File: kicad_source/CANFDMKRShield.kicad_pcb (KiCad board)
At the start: 2 copper layers, 61.5 x 25 mm, 33 parts, among them CN1 ARDUINO_MKR, CN2 CONN_01X04, CN3 GH_SM04B-GHS-TB, CN4 GH_SM04B-GHS-TB, SW1 JS202011JCQN, U1 MCP2517FD, U2 SN65HVD232, U3 TPS54232, Y1 20MHz

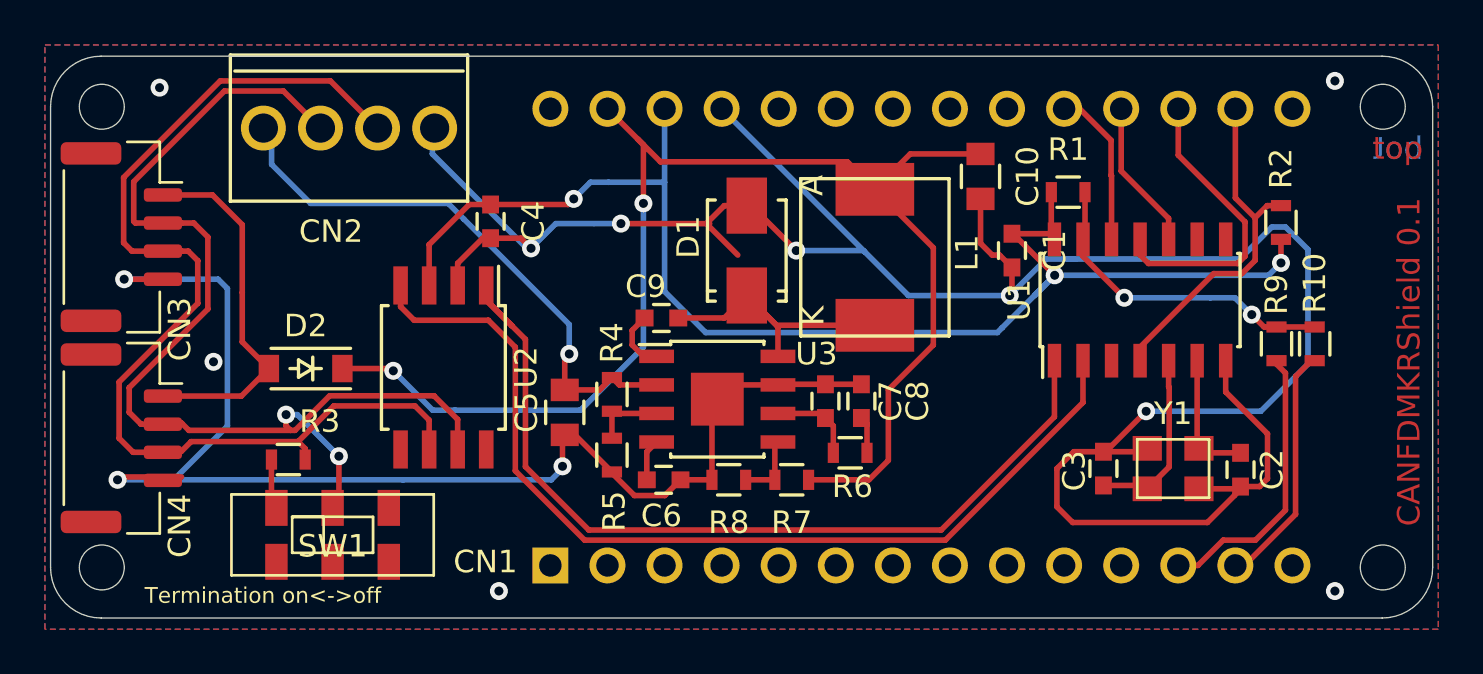
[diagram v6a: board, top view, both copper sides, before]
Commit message: updated layout
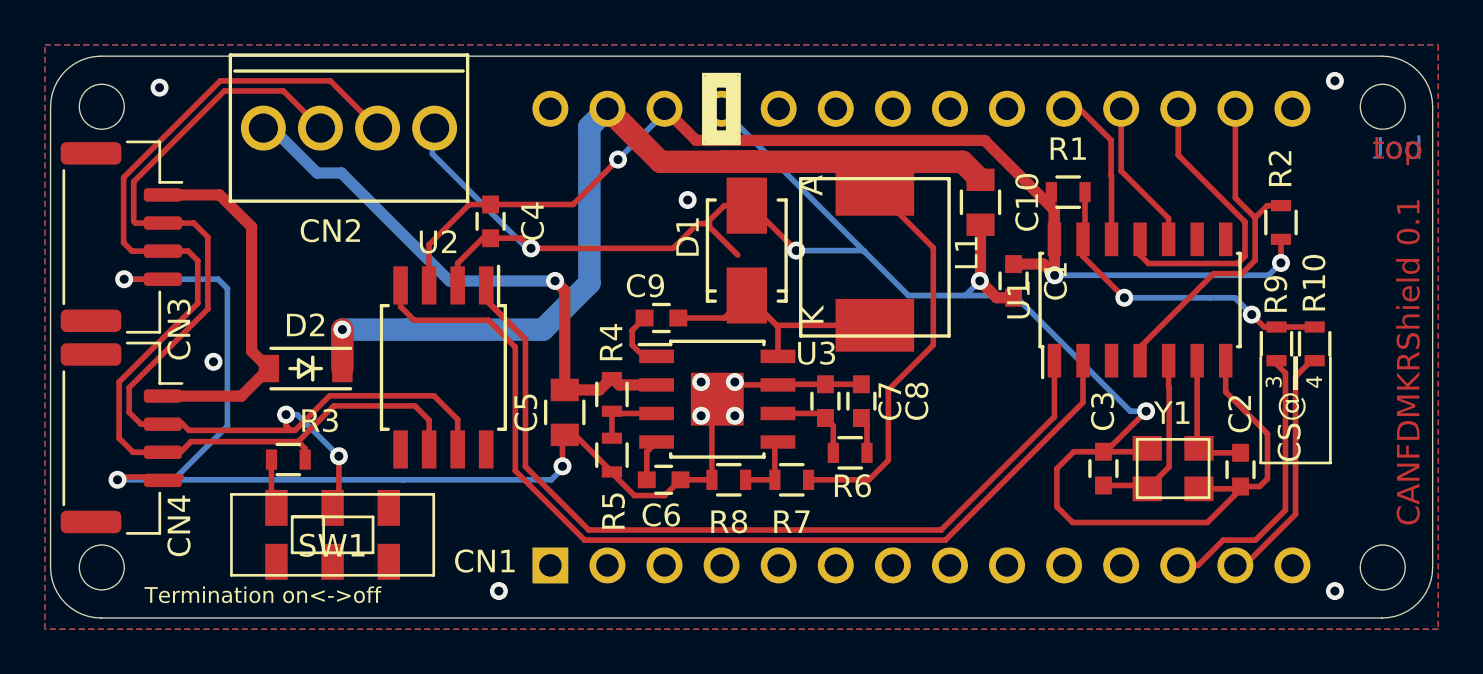
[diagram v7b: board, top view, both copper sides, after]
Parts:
- moved C1 1.35 mm to (150.1, 97.5)
- moved C10 1.15 mm to (148.6, 94.0)
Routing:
- net GND: track 167.7 -> 147.6 mm, vias 13 -> 17
- net +5V: track 61.3 -> 69.9 mm, vias 2 -> 1
- net +3V3: track 60.2 -> 52.6 mm
- net /CANVCC: track 15.4 -> 16.4 mm
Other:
- board text added: "3"
- board text added: "4"
- board text added: "CS@"

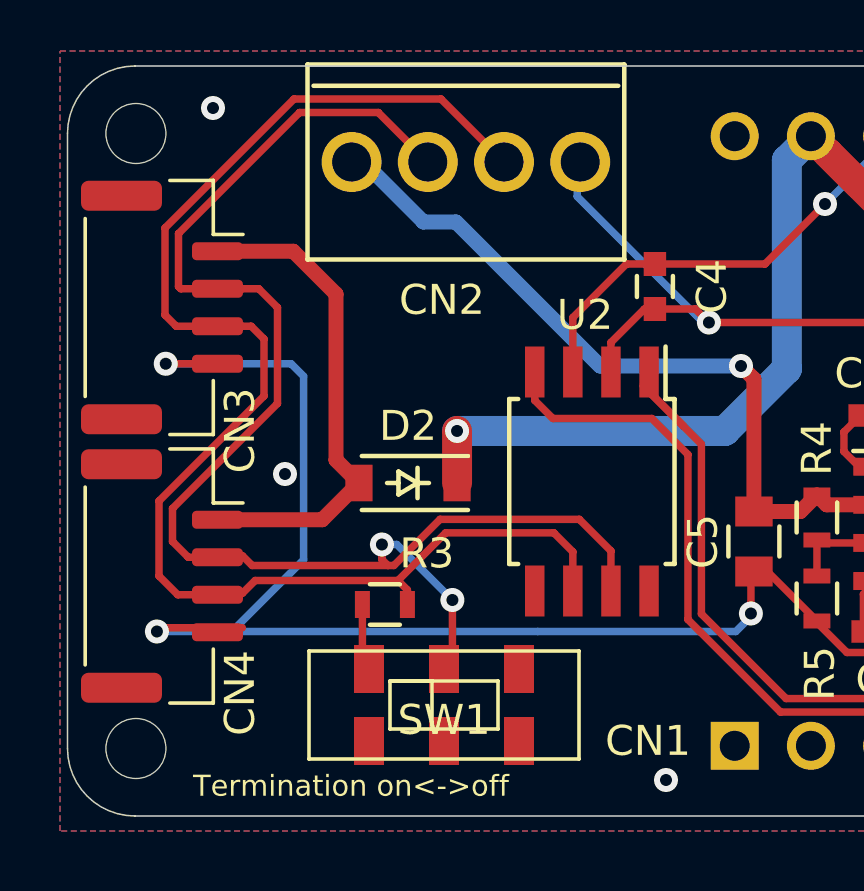
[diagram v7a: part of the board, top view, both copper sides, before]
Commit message: added some labels, updated images and schematic pdf
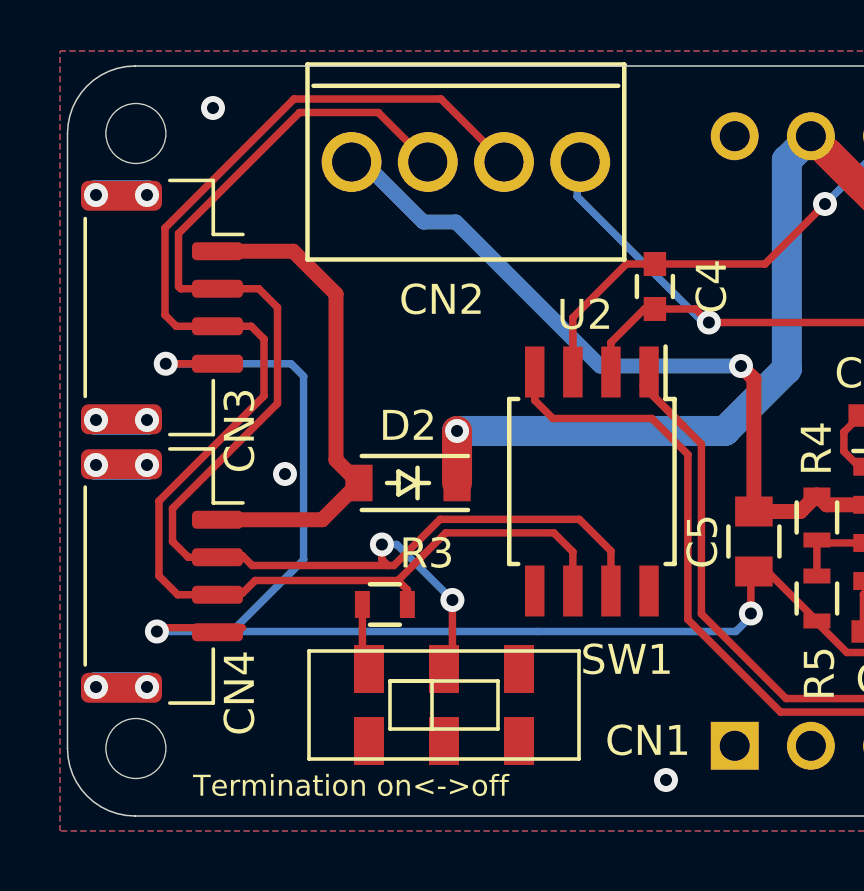
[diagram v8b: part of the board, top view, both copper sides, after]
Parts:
- added L3: Label, labels:generationmake_logo, B.Cu at (145.3, 99.8)
- Y1: value 20MHz -> RH100-20.000-20-3030-TR
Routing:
- net (no net): track 0.00 -> 6.80 mm, vias 0 -> 8
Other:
- board text added: "CANFDMKRShield"
- board text added: "CANH"
- board text added: "CANL"
- board text added: "GND"
- board text added: "VCC"
- board text added: "find more information on https://github.com/generationmake/CANFDMKRShield"
- board text added: "with Microchip MCP2517"
